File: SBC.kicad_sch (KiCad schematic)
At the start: 0 parts

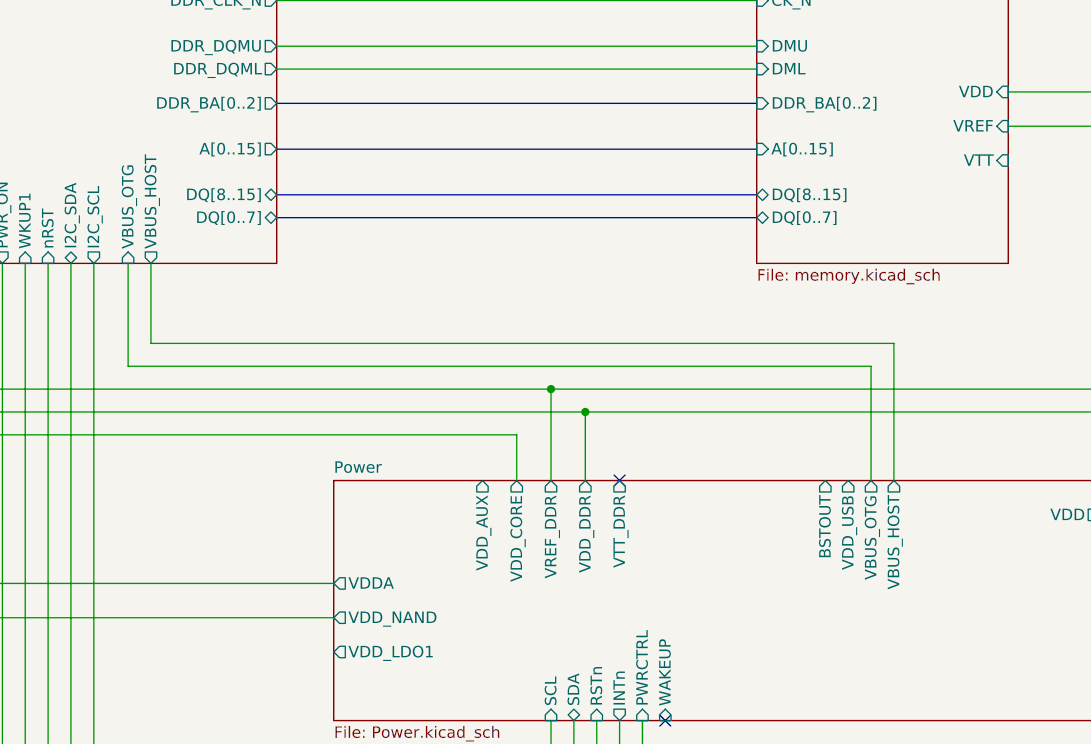
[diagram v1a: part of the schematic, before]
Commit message: Updating VDD_USB
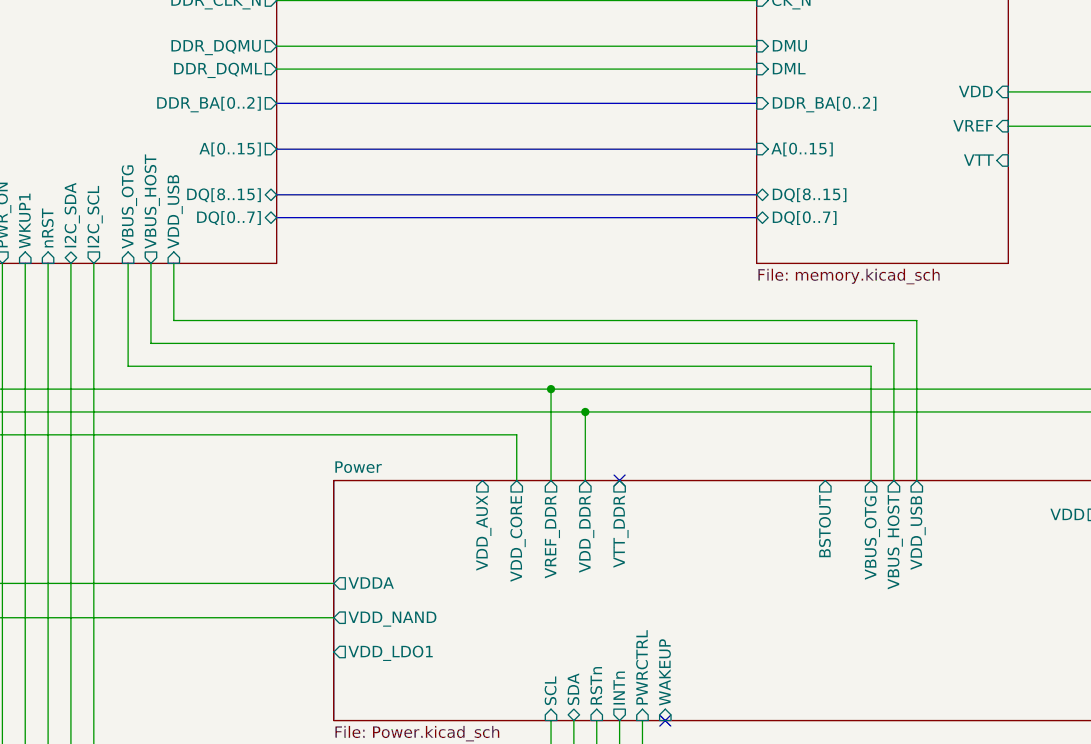
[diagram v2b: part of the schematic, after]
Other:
- sheet MPU ports: added VDD_USB; removed none
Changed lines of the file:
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@@
+	(wire
+		(pts
+			(xy 217.17 148.59) (xy 217.17 142.24)
+		)
+		(stroke
+			(width 0)
+			(type default)
+		)
+	)
 	(wire
 		(pts
@@
 	(wire
 		(pts
+			(xy 299.72 166.37) (xy 299.72 148.59)
+		)
+		(stroke
+			(width 0)
+			(type default)
+		)
+	)
+	(wire
+		(pts
 			(xy 262.89 158.75) (xy 173.99 158.75)
+		)
+		(stroke
+			(width 0)
+			(type default)
+		)
+	)
+	(wire
+		(pts
+			(xy 299.72 148.59) (xy 217.17 148.59)
 		)
 		(stroke
@@
 			)
 		)
+		(pin "VDD_USB" input
+			(at 217.17 142.24 270)
+			(effects
+				(font
+					(size 1.27 1.27)
+				)
+				(justify left)
+			)
+		)
 		(instances
 			(project "SBC"
@@
 		)
 		(pin "VDD_USB" output
-			(at 292.1 166.37 90)
-			(effects
-				(font
+			(at 299.72 166.37 90)
+			(effects
+				(font

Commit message: Started an entire reroute
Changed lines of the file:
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@@
 (kicad_sch
-	(version 20231120)
+	(version 20250114)
 	(generator "eeschema")
-	(generator_version "8.0")
+	(generator_version "9.0")
 	(paper "B")
 	(title_block
@@
 		(comment 3 "Single Board Computer")
 	)
+	(text "Notes"
+		(exclude_from_sim no)
+		(at 337.058 18.796 0)
+		(effects
+			(font
+				(face "Courier New")
+				(size 1.27 1.27)
+				(color 255 255 0 1)
+			)
+		)
+	)
+	(text_box "Trace width and spacing requirements:\n\n(Differential)\n1. 90 Ohm outer layer     -> W=0.1422mm, S=0.0994\n2. 100 Ohm outer layer    -> W=0.1095, S=0.0994\n3. 90 Ohm inner layer     -> W=0.1328, S=0.0994\n4. 100 Ohm innder layer   -> W=0.1029, S=0.0994\n\n(Single Ended)\n1. 45 Ohm outer layer     -> W=0.1542, T=0.0994\n2. 50 Ohm outer layer     -> W=0.1196, T=0.0994\n3. 55 Ohm outer layer     -> W=0.0922, T=0.0994\n4. 45 Ohm inner layer     -> W=0.1765, T=0.0994\n5. 50 Ohm inner layer     -> W=0.1425, T=0.0994\n6. 55 Ohm inner layer     -> W=0.1153, T=0.0994\n\nStack Up:\nLayer         Material                            Thickness (mm)\n\nL1            Outer Copper Weight 1.0oz           0.0350\nPrepreg       3313 RC57% 4.2mil                   0.0994\nL2            Inner Copper Weight 0.5oz           0.0152\nCore          0.55mm H/Hwithout copper            0.5500\nL3            Inner Copper Weight                 0.0152\nPrepreg       2116 RC54% 4.9mil                   0.1088\nL4            Inner Copper Weight                 0.0152\nCore          0.55mm H/Hwithout copper            0.5500\nL5            Inner Copper Weight                 0.0152\nPrepeg        3313 RC57% 4.2mil                   0.0994\nL6            Outer RC57% 4.2mil                  0.0350"
+		(exclude_from_sim no)
+		(at 334.01 19.05 0)
+		(size 81.28 64.77)
+		(margins 0.9525 0.9525 0.9525 0.9525)
+		(stroke
+			(width 0)
+			(type default)
+			(color 255 255 0 1)
+		)
+		(fill
+			(type none)
+		)
+		(effects
+			(font
+				(face "Courier New")
+				(size 1.27 1.27)
+				(color 255 255 0 1)
+			)
+			(justify left top)
+		)
+	)
 	(junction
 		(at 262.89 158.75)
@@
 		)
 	)
-	(text_box "Trace width and spacing requirements:\n\n(Differential)\n1. 90 Ohm outer layer     -> W=0.1422mm, S=0.0994\n2. 100 Ohm outer layer    -> W=0.1095, S=0.0994\n3. 90 Ohm inner layer     -> W=0.1328, S=0.0994\n4. 100 Ohm innder layer   -> W=0.1029, S=0.0994\n\n(Single Ended)\n1. 45 Ohm outer layer     -> W=0.1542, T=0.0994\n2. 50 Ohm outer layer     -> W=0.1196, T=0.0994\n3. 55 Ohm outer layer     -> W=0.0922, T=0.0994\n4. 45 Ohm inner layer     -> W=0.1765, T=0.0994\n5. 50 Ohm inner layer     -> W=0.1425, T=0.0994\n6. 55 Ohm inner layer     -> W=0.1153, T=0.0994\n\nStack Up:\nLayer         Material                            Thickness (mm)\n\nL1            Outer Copper Weight 1.0oz           0.0350\nPrepreg       3313 RC57% 4.2mil                   0.0994\nL2            Inner Copper Weight 0.5oz           0.0152\nCore          0.55mm H/Hwithout copper            0.5500\nL3            Inner Copper Weight                 0.0152\nPrepreg       2116 RC54% 4.9mil                   0.1088\nL4            Inner Copper Weight                 0.0152\nCore          0.55mm H/Hwithout copper            0.5500\nL5            Inner Copper Weight                 0.0152\nPrepeg        3313 RC57% 4.2mil                   0.0994\nL6            Outer RC57% 4.2mil                  0.0350"
-		(exclude_from_sim no)
-		(at 334.01 19.05 0)
-		(size 81.28 64.77)
-		(stroke
-			(width 0)
-			(type default)
-			(color 255 255 0 1)
-		)
-		(fill
-			(type none)
-		)
-		(effects
-			(font
-				(face "Courier New")
-				(size 1.27 1.27)
-				(color 255 255 0 1)
-			)
-			(justify left top)
-		)
-	)
-	(text "Notes"
-		(exclude_from_sim no)
-		(at 337.058 18.796 0)
-		(effects
-			(font
-				(face "Courier New")
-				(size 1.27 1.27)
-				(color 255 255 0 1)
-			)
-		)
-	)
 	(netclass_flag ""
 		(length 0.0254)
@@
 		(at 281.94 38.1)
 		(size 27.94 104.14)
+		(exclude_from_sim no)
+		(in_bom yes)
+		(on_board yes)
+		(dnp no)
 		(fields_autoplaced yes)
 		(stroke
@@
 		(at 179.07 38.1)
 		(size 49.53 104.14)
+		(exclude_from_sim no)
+		(in_bom yes)
+		(on_board yes)
+		(dnp no)
 		(fields_autoplaced yes)
 		(stroke
@@
 		(at 234.95 166.37)
 		(size 85.09 26.67)
+		(exclude_from_sim no)
+		(in_bom yes)
+		(on_board yes)
+		(dnp no)
 		(fields_autoplaced yes)
 		(stroke
@@
 		(at 105.41 106.68)
 		(size 41.91 36.83)
+		(exclude_from_sim no)
+		(in_bom yes)
+		(on_board yes)
+		(dnp no)
 		(fields_autoplaced yes)
 		(stroke
@@
 		(at 105.41 38.1)
 		(size 41.91 59.69)
+		(exclude_from_sim no)
+		(in_bom yes)
+		(on_board yes)
+		(dnp no)
 		(fields_autoplaced yes)
 		(stroke
@@
 		)
 	)
+	(embedded_fonts no)
 )

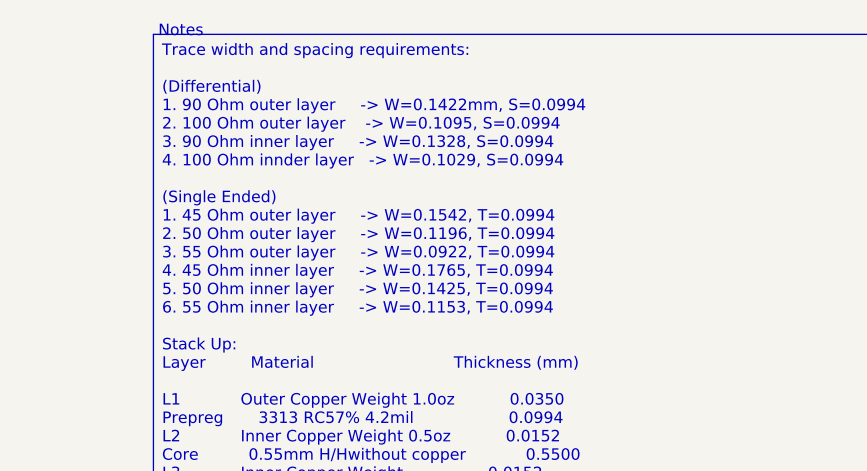
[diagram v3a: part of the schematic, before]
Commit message: DDR Routing commenced
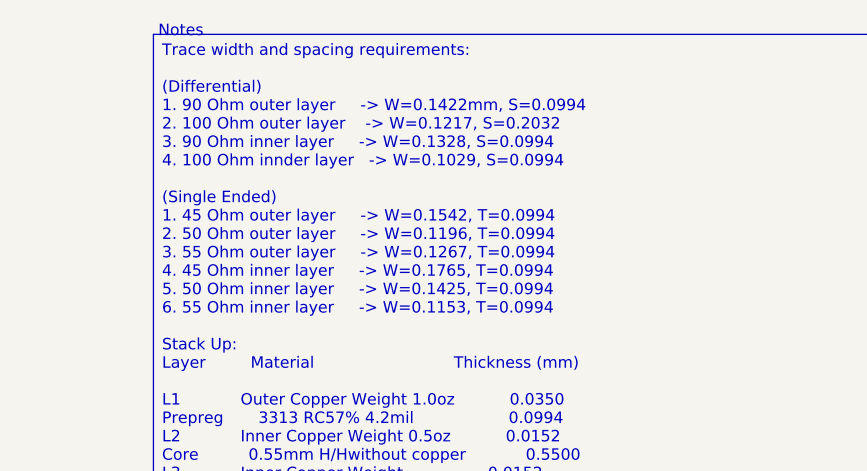
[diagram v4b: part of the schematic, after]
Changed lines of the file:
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@@
 		)
 	)
-	(text_box "Trace width and spacing requirements:\n\n(Differential)\n1. 90 Ohm outer layer     -> W=0.1422mm, S=0.0994\n2. 100 Ohm outer layer    -> W=0.1095, S=0.0994\n3. 90 Ohm inner layer     -> W=0.1328, S=0.0994\n4. 100 Ohm innder layer   -> W=0.1029, S=0.0994\n\n(Single Ended)\n1. 45 Ohm outer layer     -> W=0.1542, T=0.0994\n2. 50 Ohm outer layer     -> W=0.1196, T=0.0994\n3. 55 Ohm outer layer     -> W=0.0922, T=0.0994\n4. 45 Ohm inner layer     -> W=0.1765, T=0.0994\n5. 50 Ohm inner layer     -> W=0.1425, T=0.0994\n6. 55 Ohm inner layer     -> W=0.1153, T=0.0994\n\nStack Up:\nLayer         Material                            Thickness (mm)\n\nL1            Outer Copper Weight 1.0oz           0.0350\nPrepreg       3313 RC57% 4.2mil                   0.0994\nL2            Inner Copper Weight 0.5oz           0.0152\nCore          0.55mm H/Hwithout copper            0.5500\nL3            Inner Copper Weight                 0.0152\nPrepreg       2116 RC54% 4.9mil                   0.1088\nL4            Inner Copper Weight                 0.0152\nCore          0.55mm H/Hwithout copper            0.5500\nL5            Inner Copper Weight                 0.0152\nPrepeg        3313 RC57% 4.2mil                   0.0994\nL6            Outer RC57% 4.2mil                  0.0350"
+	(text_box "Trace width and spacing requirements:\n\n(Differential)\n1. 90 Ohm outer layer     -> W=0.1422mm, S=0.0994\n2. 100 Ohm outer layer    -> W=0.1217, S=0.2032\n3. 90 Ohm inner layer     -> W=0.1328, S=0.0994\n4. 100 Ohm innder layer   -> W=0.1029, S=0.0994\n\n(Single Ended)\n1. 45 Ohm outer layer     -> W=0.1542, T=0.0994\n2. 50 Ohm outer layer     -> W=0.1196, T=0.0994\n3. 55 Ohm outer layer     -> W=0.1267, T=0.0994\n4. 45 Ohm inner layer     -> W=0.1765, T=0.0994\n5. 50 Ohm inner layer     -> W=0.1425, T=0.0994\n6. 55 Ohm inner layer     -> W=0.1153, T=0.0994\n\nStack Up:\nLayer         Material                            Thickness (mm)\n\nL1            Outer Copper Weight 1.0oz           0.0350\nPrepreg       3313 RC57% 4.2mil                   0.0994\nL2            Inner Copper Weight 0.5oz           0.0152\nCore          0.55mm H/Hwithout copper            0.5500\nL3            Inner Copper Weight                 0.0152\nPrepreg       2116 RC54% 4.9mil                   0.1088\nL4            Inner Copper Weight                 0.0152\nCore          0.55mm H/Hwithout copper            0.5500\nL5            Inner Copper Weight                 0.0152\nPrepeg        3313 RC57% 4.2mil                   0.0994\nL6            Outer RC57% 4.2mil                  0.0350"
 		(exclude_from_sim no)
 		(at 334.01 19.05 0)
@@
 		(stroke
 			(width 0)
-			(type default)
+			(type solid)
 			(color 255 255 0 1)
 		)

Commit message: Routing Eth
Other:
- sheet Ethernet ports: added none; removed ETH_CLK
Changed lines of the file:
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@@
-	(wire
-		(pts
-			(xy 147.32 48.26) (xy 179.07 48.26)
-		)
-		(stroke
-			(width 0)
-			(type default)
-		)
-	)
 	(wire
 		(pts
@@
 		(property "Netclass" "RMII"
 			(at 150.4696 63.4746 0)
-			(effects
-				(font
-					(size 1.27 1.27)
-					(italic yes)
-				)
-				(justify left)
-			)
-		)
-	)
-	(netclass_flag ""
-		(length 0.0254)
-		(shape round)
-		(at 149.86 48.26 0)
-		(fields_autoplaced yes)
-		(effects
-			(font
-				(size 1.27 1.27)
-			)
-			(justify left bottom)
-		)
-		(property "Netclass" "RMII"
-			(at 150.4696 48.2346 0)
 			(effects
 				(font
@@
 			(effects
 				(font
-					(size 1.27 1.27)
-				)
-				(justify right)
-			)
-		)
-		(pin "ETH_CLK" input
-			(at 147.32 48.26 0)
-			(effects
-				(font

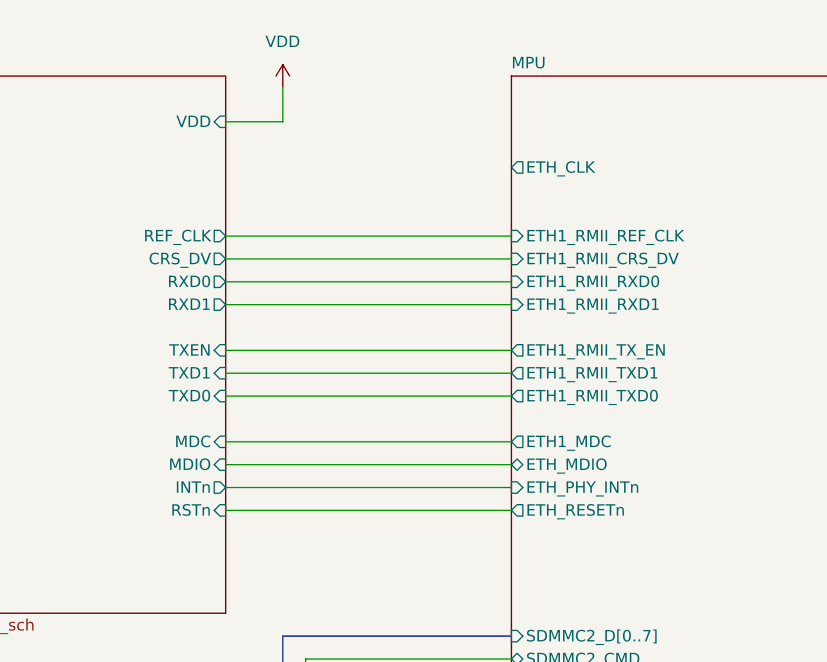
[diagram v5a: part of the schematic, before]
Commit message: Routing power and fixing minor things
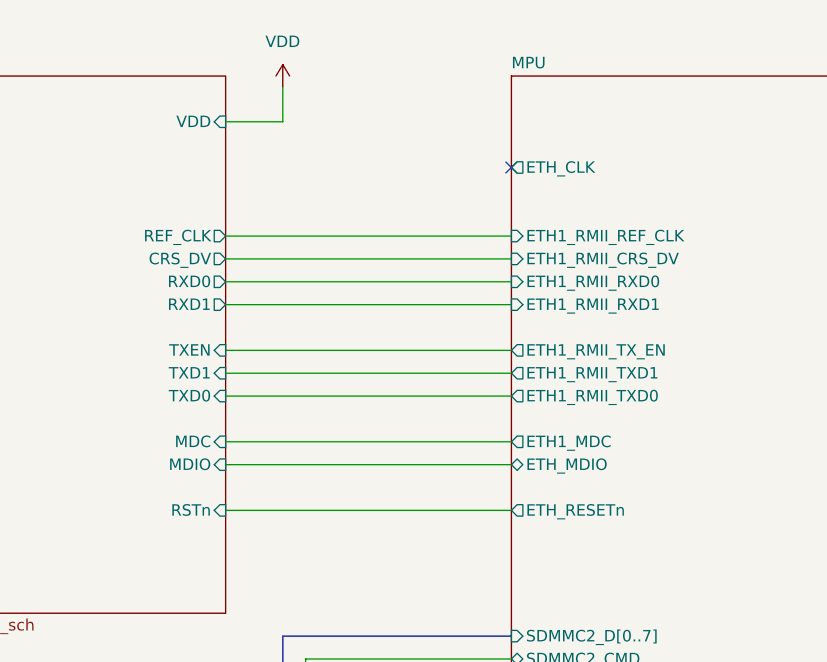
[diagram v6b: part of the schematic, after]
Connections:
- no-connect marks 3 -> 4
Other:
- sheet Ethernet ports: added none; removed INTn
- sheet MPU ports: added none; removed ETH_PHY_INTn
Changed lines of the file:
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@@
+	)
+	(no_connect
+		(at 179.07 48.26)
 	)
 	(no_connect
@@
 		(pts
 			(xy 228.6 134.62) (xy 281.94 134.62)
-		)
-		(stroke
-			(width 0)
-			(type default)
-		)
-	)
-	(wire
-		(pts
-			(xy 147.32 83.82) (xy 179.07 83.82)
 		)
 		(stroke
@@
 			)
 		)
-		(pin "ETH_PHY_INTn" input
-			(at 179.07 83.82 180)
-			(effects
-				(font
-					(size 1.27 1.27)
-				)
-				(justify left)
-			)
-		)
 		(pin "ETH_MDIO" bidirectional
 			(at 179.07 81.28 180)
@@
 			(effects
 				(font
-					(size 1.27 1.27)
-				)
-				(justify right)
-			)
-		)
-		(pin "INTn" output
-			(at 147.32 83.82 0)
-			(effects
-				(font

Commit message: Fixing errors
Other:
- note added: "EMMC"
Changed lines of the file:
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@@
+		)
+	)
+	(text "EMMC"
+		(exclude_from_sim no)
+		(at 166.37 107.188 0)
+		(effects
+			(font
+				(size 1.27 1.27)
+			)
 		)
 	)
@@
 			)
 		)
-	)
-	(netclass_flag ""
-		(length 0.0254)
-		(shape round)
-		(at 162.56 107.95 0)
-		(effects
-			(font
-				(size 1.27 1.27)
-			)
-			(justify left bottom)
-		)
-		(property "Netclass" "EMMC"
-			(at 163.1696 107.9246 0)
-			(effects
-				(font
-					(size 1.27 1.27)
-					(italic yes)
-				)
-				(justify left bottom)
-			)
-		)
